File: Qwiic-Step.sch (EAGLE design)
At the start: 54 parts, among them J1 PTH, J2 Qwiic Right Angle, J3 POWER_JACKSUPER_BOMB_DIGITY, J4 Qwiic Right Angle, J5 ISP, U1 A49885MM, U2 ATMEGA328P_TQFP, Y1 16MHz

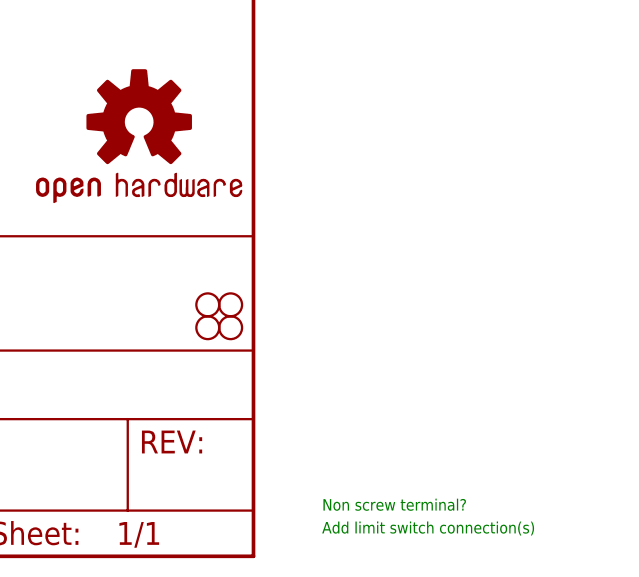
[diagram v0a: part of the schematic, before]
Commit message: Add limit switches
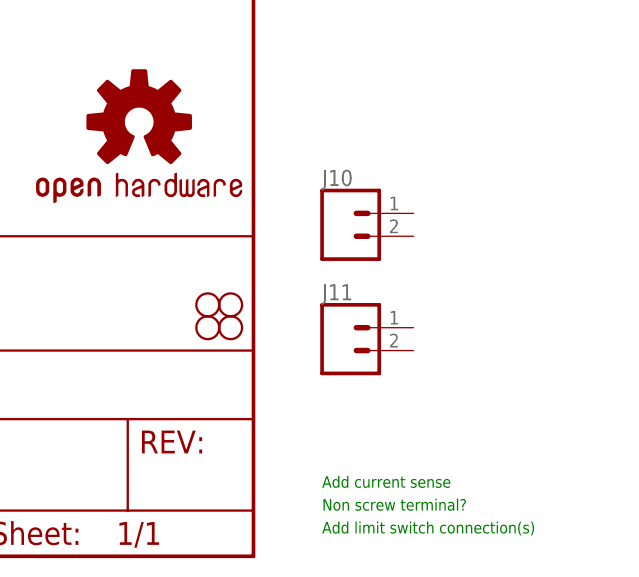
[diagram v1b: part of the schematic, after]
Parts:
- added J10, J11: (no value), SparkFun-Connectors:CONN_02-JST-2MM-SMT
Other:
- note added: "Add current sense"
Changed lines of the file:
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@@
 <part name="SUPPLY5" library="SparkFun-PowerSymbols" deviceset="3.3V" device=""/>
 <part name="J8" library="SparkFun-Connectors" deviceset="CONN_01" device="PTH_NO_SILK_YES_STOP"/>
+<part name="J10" library="SparkFun-Connectors" deviceset="CONN_02" device="-JST-2MM-SMT"/>
+<part name="J11" library="SparkFun-Connectors" deviceset="CONN_02" device="-JST-2MM-SMT"/>
 </parts>
 <sheets>
@@
 <text x="73.66" y="12.7" size="1.27" layer="91">TXO</text>
 <text x="73.66" y="10.16" size="1.27" layer="91">RXI</text>
+<text x="256.54" y="7.62" size="1.27" layer="91">Add current sense</text>
 </plain>
 <instances>
@@
 <attribute name="NAME" x="139.7" y="22.352" size="1.778" layer="95" font="vector" rot="R180"/>
 </instance>
+<instance part="J10" gate="G$1" x="259.08" y="35.56" smashed="yes">
+<attribute name="VALUE" x="256.54" y="30.734" size="1.778" layer="96" font="vector"/>
+<attribute name="NAME" x="256.54" y="41.148" size="1.778" layer="95" font="vector"/>
+</instance>
+<instance part="J11" gate="G$1" x="259.08" y="22.86" smashed="yes">
+<attribute name="VALUE" x="256.54" y="18.034" size="1.778" layer="96" font="vector"/>
+<attribute name="NAME" x="256.54" y="28.448" size="1.778" layer="95" font="vector"/>
+</instance>
 </instances>
